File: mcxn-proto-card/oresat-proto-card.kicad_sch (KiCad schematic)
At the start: 16 parts, among them J1 J-SAMTEC-TFM-120-X1-XXX-D-RA, J2 J-SAMTEC-TFM-110-01-L-D-RA, J3 SM14B-SHLS-TF, J4 2477330-1, J5 2477330-1, J6 2477330-1, J7 U.FL-R-SMT-1(10), J8 U.FL-R-SMT-1(10), J9 U.FL-R-SMT-1(10)

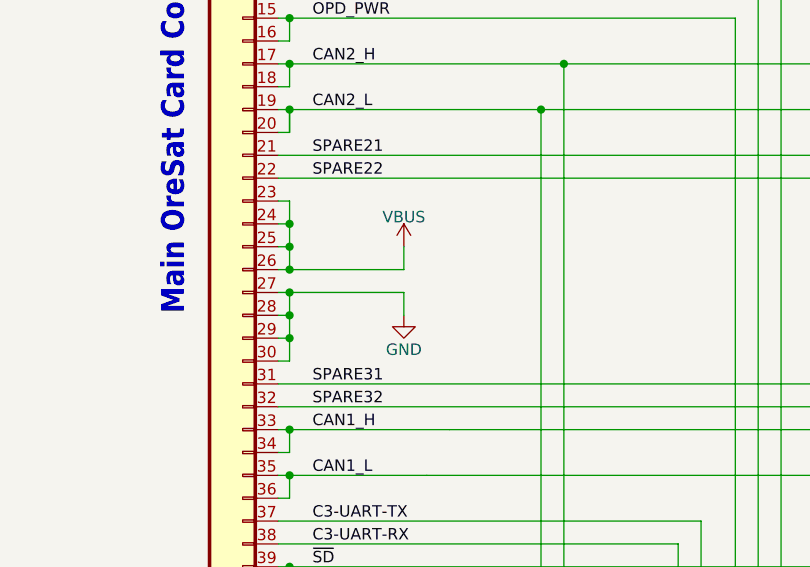
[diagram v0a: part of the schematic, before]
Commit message: Fixed version pins and lots of ref des formatting; BOM still not right.
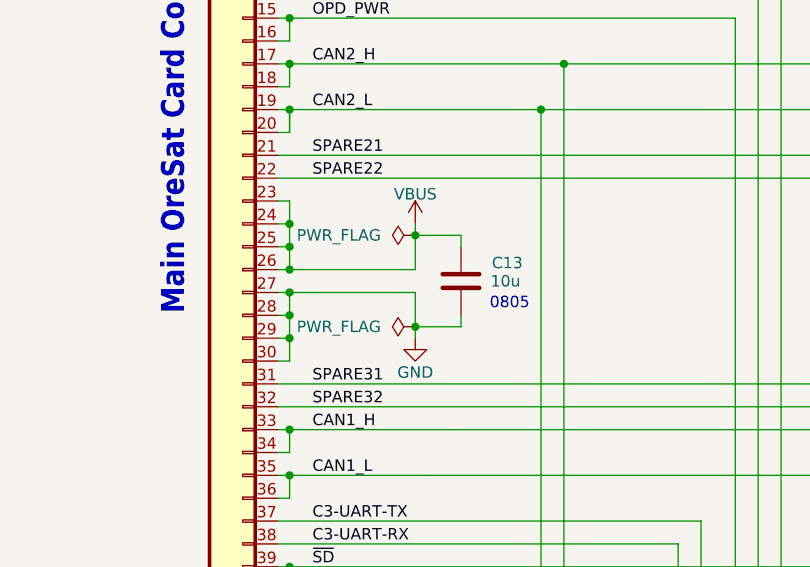
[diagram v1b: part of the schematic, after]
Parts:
- added C13: 10u, oresat-passives:0805-B-NOSILK, symbol Device:C
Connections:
- net GND: now also C13.2
- net VBUS: now also C13.1
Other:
- note added: "0805"

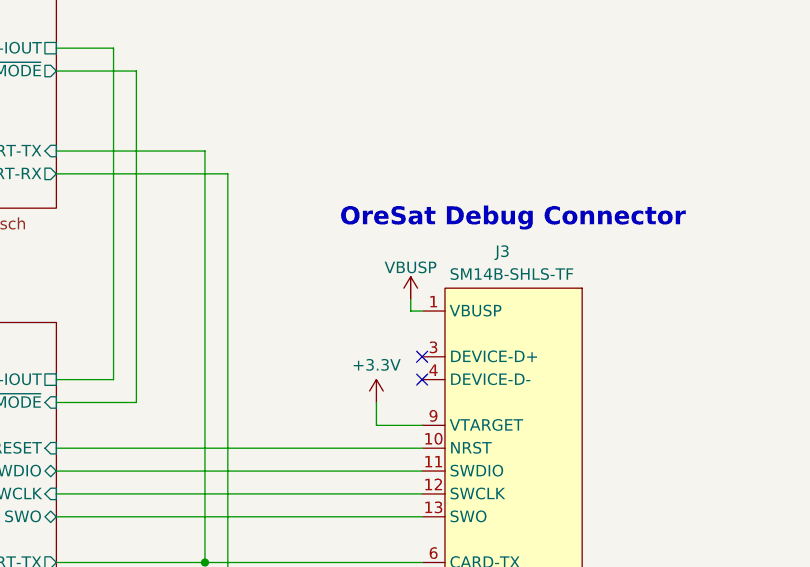
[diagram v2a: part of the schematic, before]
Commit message: Updated v6.2 date, fixed ERCs using power flags, fixed DRCs using custom rules and fixes. Should be good to go.
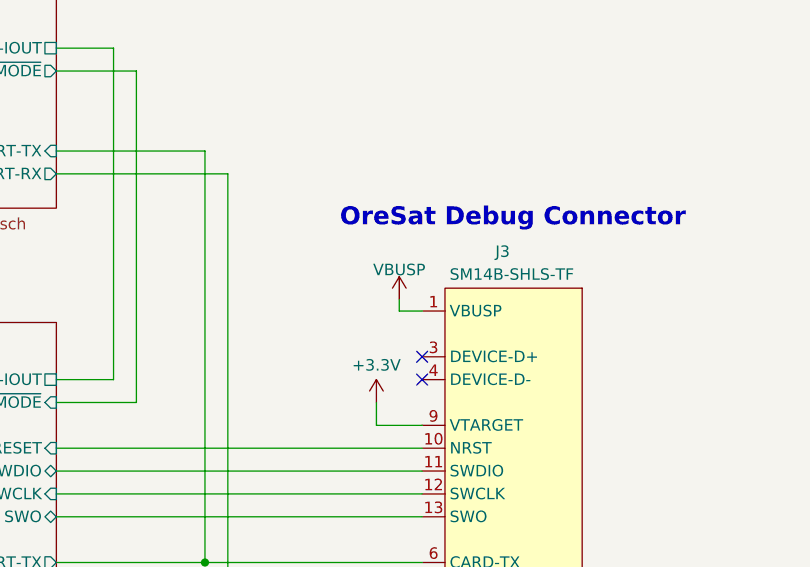
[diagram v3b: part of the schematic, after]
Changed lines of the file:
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@@
 	(title_block
 		(title "OreSat MCXN Proto Card")
-		(date "2026-10-19")
+		(date "2026-10-21")
 		(rev "6.2")
 		(company "Portland State Aerospace Society")
@@
 	(wire
 		(pts
-			(xy 100.33 162.56) (xy 111.76 162.56)
+			(xy 191.77 180.34) (xy 189.23 180.34)
 		)
 		(stroke
-			(width 0.1524)
-			(type solid)
+			(width 0)
+			(type default)
 		)
 	)
 	(wire
 		(pts
-			(xy 53.34 99.06) (xy 54.61 99.06)
+			(xy 100.33 162.56) (xy 111.76 162.56)
 		)
 		(stroke
@@
 	(wire
 		(pts
-			(xy 190.5 180.34) (xy 191.77 180.34)
+			(xy 53.34 99.06) (xy 54.61 99.06)
 		)
 		(stroke
-			(width 0)
-			(type default)
+			(width 0.1524)
+			(type solid)
 		)
 	)
@@
 	(wire
 		(pts
-			(xy 190.5 179.07) (xy 190.5 180.34)
-		)
-		(stroke
-			(width 0)
-			(type default)
-		)
-	)
-	(wire
-		(pts
 			(xy 53.34 127) (xy 54.61 127)
 		)
@@
 	(wire
 		(pts
+			(xy 189.23 180.34) (xy 189.23 179.07)
+		)
+		(stroke
+			(width 0)
+			(type default)
+		)
+	)
+	(wire
+		(pts
 			(xy 297.18 63.5) (xy 297.18 60.96)
 		)
@@
 	)
 	(symbol
+		(lib_id "oresat-power:VBUS")
+		(at 189.23 179.07 0)
+		(unit 1)
+		(body_style 1)
+		(exclude_from_sim no)
+		(in_bom yes)
+		(on_board yes)
+		(in_pos_files yes)
+		(dnp no)
+		(property "Reference" "#VBUS05"
+			(at 189.23 182.88 0)
+			(hide yes)
+			(show_name no)
+			(do_not_autoplace no)
+			(effects
+				(font
+					(size 1.27 1.27)
+				)
+			)
+		)
+		(property "Value" "VBUSP"
+			(at 189.23 175.768 0)
+			(show_name no)
+			(do_not_autoplace no)
+			(effects
+				(font
+					(size 1.27 1.27)
+				)
+			)
+		)
+		(property "Footprint" ""
+			(at 189.23 179.07 0)
+			(hide yes)
+			(show_name no)
+			(do_not_autoplace no)
+			(effects
+				(font
+					(size 1.27 1.27)
+				)
+			)
+		)
+		(property "Datasheet" ""
+			(at 189.23 179.07 0)
+			(hide yes)
+			(show_name no)
+			(do_not_autoplace no)
+			(effects
+				(font
+					(size 1.27 1.27)
+				)
+			)
+		)
+		(property "Description" ""
+			(at 189.23 179.07 0)
+			(show_name no)
+			(do_not_autoplace no)
+			(effects
+				(font
+					(size 1.27 1.27)
+				)
+			)
+		)
+		(pin "1"
+		)
+		(instances
+			(project "oresat-proto-card"
+				(path "/04d32576-d084-475b-9eac-d7f3fd9579d7"
+					(reference "#VBUS05")
+					(unit 1)
+				)
+			)
+		)
+	)
+	(symbol
 		(lib_id "power:+3.3V")
 		(at 186.69 190.5 0)
@@
 					(unit 1)
 				)
-			)
-		)
-	)
-	(symbol
-		(lib_id "oresat-power:VBUSP")
-		(at 190.5 179.07 0)
-		(unit 1)
-		(body_style 1)
-		(exclude_from_sim no)
-		(in_bom yes)
-		(on_board yes)
-		(in_pos_files yes)
-		(dnp no)
-		(property "Reference" "#VBUSP01"
-			(at 190.5 179.07 0)
-			(hide yes)
-			(show_name no)
-			(do_not_autoplace no)
-			(effects
-				(font
-					(size 1.27 1.27)
-				)
-			)
-		)
-		(property "Value" "VBUSP"
-			(at 190.5 176.276 0)
-			(show_name no)
-			(do_not_autoplace no)
-			(effects
-				(font
-					(size 1.27 1.27)
-				)
-				(justify bottom)
-			)
-		)
-		(property "Footprint" ""
-			(at 190.5 179.07 0)
-			(hide yes)
-			(show_name no)
-			(do_not_autoplace no)
-			(effects
-				(font
-					(size 1.27 1.27)
-				)
-			)
-		)
-		(property "Datasheet" ""
-			(at 190.5 179.07 0)
-			(hide yes)
-			(show_name no)
-			(do_not_autoplace no)
-			(effects
-				(font
-					(size 1.27 1.27)
-				)
-			)
-		)
-		(property "Description" "Power symbol creates a global label with name \"VBUSP\""
-			(at 190.5 179.07 0)
-			(hide yes)
-			(show_name no)
-			(do_not_autoplace no)
-			(effects
-				(font
-					(size 1.27 1.27)
-				)
-			)
-		)
-		(pin "1"
-		)
-		(instances
-			(project "oresat-proto-card"
-				(path "/04d32576-d084-475b-9eac-d7f3fd9579d7"
-					(reference "#VBUSP01")
-					(unit 1)
-				)
